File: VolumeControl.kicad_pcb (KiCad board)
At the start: 2 copper layers, 36 parts, among them J1 Input R/GND/L, J2 SPI, J4 5V Supply, J5 Lout, J6 Rout, J7 SubOut, U1 AD8400ARZ100, U2 AD8400ARZ100, U3 TL082, U4 TL082

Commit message: ähhhh
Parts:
- moved J4 128.4 mm to (27.4, 32.5), turned to 180 degrees
- moved C2 95.9 mm to (161.5, 30.5), turned to -90 degrees
- moved C3 89.6 mm to (135.4, 39.1), turned to 180 degrees
- moved C1 86.5 mm to (147.9, 24.4), turned to 90 degrees
- moved R2 84.6 mm to (128.5, 31.5)
- moved R1 82.1 mm to (138.7, 23.9), turned to 180 degrees
- moved R3 80.3 mm to (142.2, 33.5), turned to 90 degrees
- moved R4 78.2 mm to (151.9, 40.6)
- moved J1 70.5 mm to (161.4, 24.4), turned to 180 degrees
- moved R14 67.8 mm to (139.3, 104.9), turned to 180 degrees
- moved C4 66.6 mm to (42.4, 38.6), turned to 180 degrees
- moved C7 63.7 mm to (84.7, 33.5), turned to 90 degrees
- moved R12 59.2 mm to (80.9, 36.2), turned to 180 degrees
- moved U1 59.2 mm to (78.7, 59.9)
- moved C6 58.9 mm to (116.9, 124.0)
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
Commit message: uf
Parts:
- moved C2 29.5 mm to (135.2, 17.3), turned to 0 degrees
- moved R2 29.2 mm to (146.8, 54.2), turned to 90 degrees
- moved C7 26.3 mm to (72.6, 56.9)
- moved C8 26.3 mm to (72.6, 48.5)
- moved R12 26.3 mm to (68.8, 59.6)
- moved R13 26.3 mm to (58.3, 41.7)
- moved C3 20.8 mm to (154.4, 47.4), turned to -90 degrees
- moved R1 20.2 mm to (139.2, 44.0), turned to -90 degrees
- moved PS1 18.6 mm to (52.9, 36.5)
- moved C1 13.3 mm to (139.7, 34.8), turned to 180 degrees
- moved J1 12.5 mm to (148.9, 24.4), turned to -90 degrees
- moved R4 10.0 mm to (157.0, 32.0), turned to 90 degrees
- moved R3 9.59 mm to (148.8, 40.5), turned to 180 degrees
- moved U1 7.55 mm to (84.3, 54.9)
- moved U3 7.55 mm to (93.7, 84.1)
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
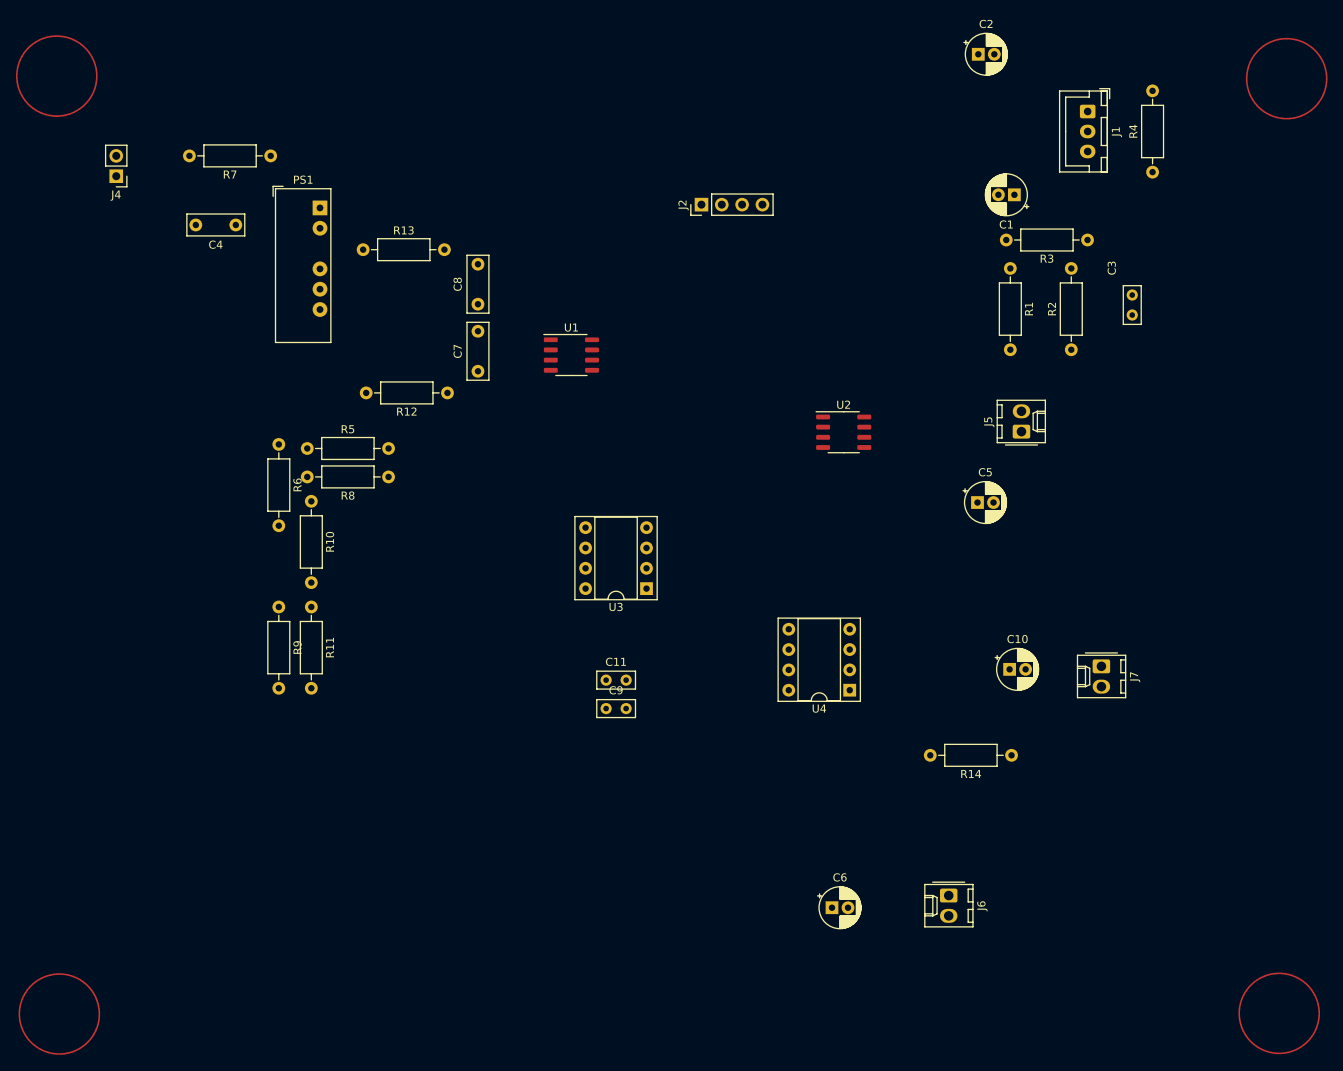
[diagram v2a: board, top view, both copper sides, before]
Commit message: corrected some issues in the schematic * added jumper for phase invert of the sub out * routed layout
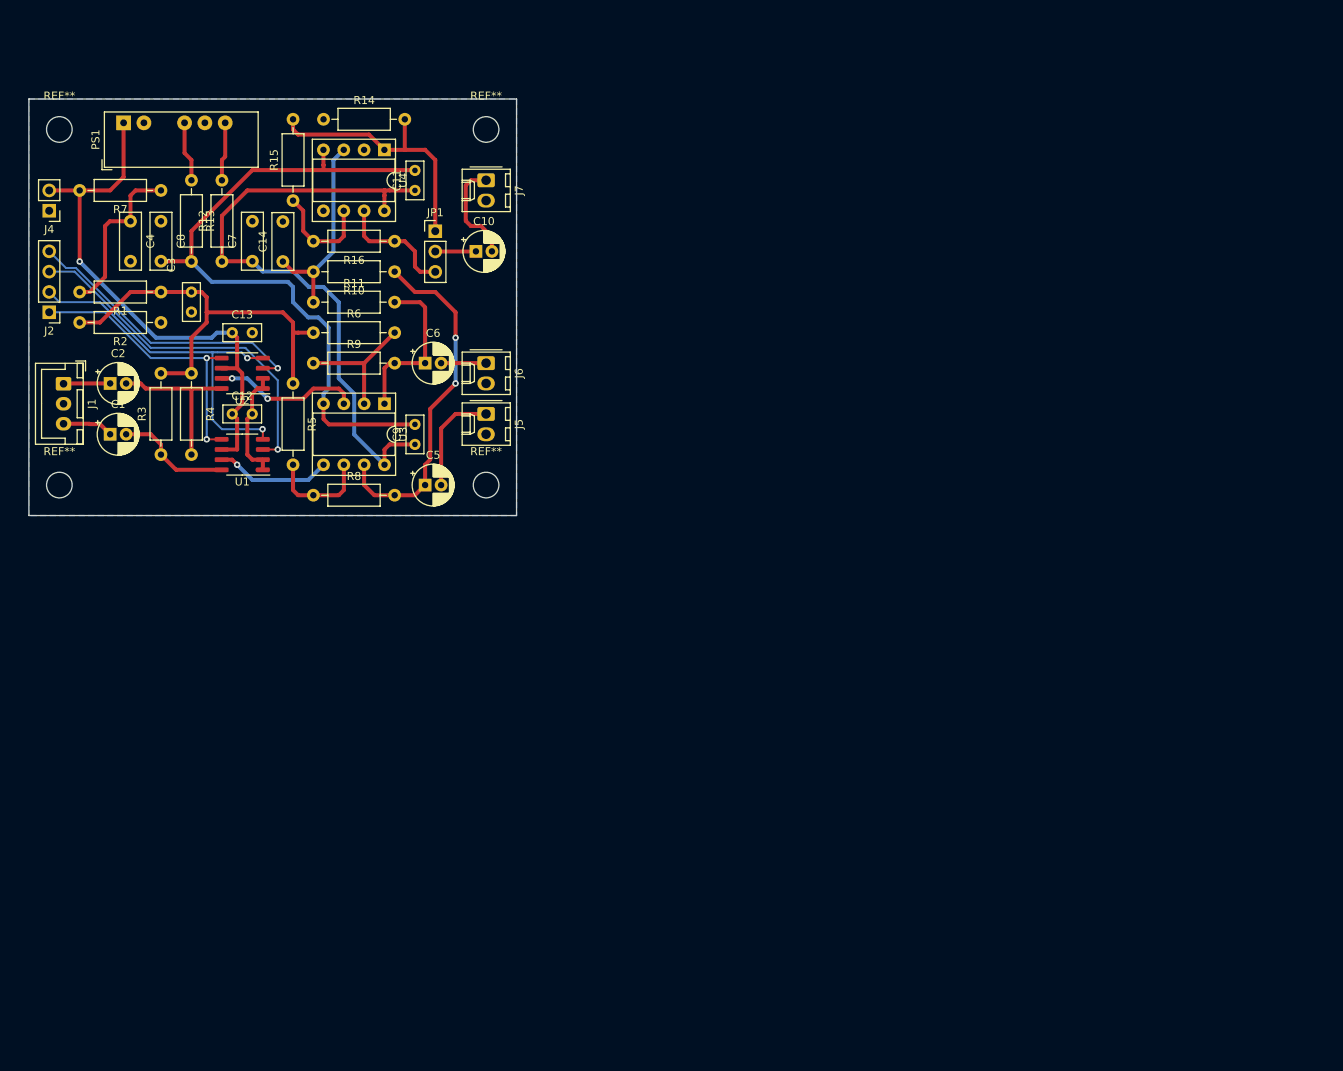
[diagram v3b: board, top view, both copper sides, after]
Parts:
- added C12: 100n, Capacitor_THT:C_Rect_L4.6mm_W2.0mm_P2.50mm_MKS02_FKP02, F.Cu at (41.9, 62.2)
- added C13: 100n, Capacitor_THT:C_Rect_L4.6mm_W2.0mm_P2.50mm_MKS02_FKP02, F.Cu at (41.9, 52.1)
- added C14: n.b., Capacitor_THT:C_Rect_L7.0mm_W2.5mm_P5.00mm, F.Cu at (48.3, 43.2)
- added JP1: Sub out invert select, Connector_PinHeader_2.54mm:PinHeader_1x03_P2.54mm_Vertical, F.Cu at (67.3, 39.4)
- added R15: 10K, Resistor_THT:R_Axial_DIN0207_L6.3mm_D2.5mm_P10.16mm_Horizontal, F.Cu at (49.5, 35.6)
- added R16: 10K, Resistor_THT:R_Axial_DIN0207_L6.3mm_D2.5mm_P10.16mm_Horizontal, F.Cu at (62.2, 40.6)
- added REF**: MountingHole_3.2mm_M3, MountingHole:MountingHole_3.2mm_M3, F.Cu at (73.7, 71.1)
- added REF**: MountingHole_3.2mm_M3, MountingHole:MountingHole_3.2mm_M3, F.Cu at (20.3, 71.1)
- added REF**: MountingHole_3.2mm_M3, MountingHole:MountingHole_3.2mm_M3, F.Cu at (73.7, 26.7)
- added REF**: MountingHole_3.2mm_M3, MountingHole:MountingHole_3.2mm_M3, F.Cu at (20.3, 26.7)
- moved J1 132.5 mm to (20.8, 58.5)
- moved R4 122.7 mm to (36.8, 57.1), turned to -90 degrees
- moved R3 118.9 mm to (33.0, 67.3), turned to 90 degrees
- moved C3 117.6 mm to (36.8, 47.0)
- moved R14 117.1 mm to (53.3, 25.4), turned to 0 degrees
- moved C1 116.9 mm to (26.7, 64.8), turned to 0 degrees
- moved C2 116.1 mm to (26.7, 58.4)
- moved R2 113.8 mm to (33.0, 50.8), turned to 180 degrees
- moved R1 106.2 mm to (33.0, 47.0), turned to 180 degrees
- moved J7 98.0 mm to (73.7, 33.0)
- moved U4 89.1 mm to (61.0, 29.2), turned to -90 degrees
- moved J6 88.2 mm to (73.7, 55.9)
- moved C6 85.0 mm to (66.0, 55.9)
- moved C10 84.7 mm to (72.4, 41.9)
- moved J2 82.6 mm to (19.1, 49.5), turned to 180 degrees
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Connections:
- C11 pad 1: Net-(C11-Pad1) -> +12VA
- C11 pad 2: Net-(C11-Pad2) -> -12VA
- C3 pad 1: Net-(C3-Pad1) -> mid
- C9 pad 1: Net-(C11-Pad1) -> +12VA
- C9 pad 2: Net-(C11-Pad2) -> -12VA
- J2 pad 2: /SDA -> /SDI
- R1 pad 1: Net-(C3-Pad1) -> mid
- R14 pad 2: Net-(C10-Pad1) -> Net-(R15-Pad2)
- R2 pad 2: Net-(C3-Pad1) -> mid
- R3 pad 2: Net-(C3-Pad1) -> mid
- R4 pad 1: Net-(C3-Pad1) -> mid
- R5 pad 1: GND -> mid
- R6 pad 1: GND -> mid
- U3 pad 4: Net-(C11-Pad2) -> -12VA
- U3 pad 8: Net-(C11-Pad1) -> +12VA
- U4 pad 1: Net-(C10-Pad1) -> Net-(R15-Pad2)
- U4 pad 4: Net-(C11-Pad2) -> -12VA
- U4 pad 5: -12VA -> GND
- U4 pad 6: +12VA -> Net-(U4-Pad6)
- U4 pad 7: unconnected-(U4-Pad7) -> Net-(U4-Pad7)
- U4 pad 8: Net-(C11-Pad1) -> +12VA
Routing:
- net -12VA: track 0.00 -> 86.4 mm
- net +12VA: track 0.00 -> 79.1 mm
- net +5V: track 0.00 -> 68.7 mm, vias 0 -> 1
- net mid: track 0.00 -> 53.3 mm
- net /SDI: track 0.00 -> 46.6 mm, vias 0 -> 2
- net /CS1: track 0.00 -> 44.7 mm, vias 0 -> 1
- net Net-(C5-Pad1): track 0.00 -> 44.1 mm, vias 0 -> 2
- net /CS2: track 0.00 -> 36.5 mm, vias 0 -> 1
- net /CLK: track 0.00 -> 36.0 mm, vias 0 -> 2
- net Net-(R15-Pad2): track 0.00 -> 33.4 mm
- net Net-(R10-Pad2): track 0.00 -> 25.0 mm
- net +5VA: track 0.00 -> 21.0 mm
- net Net-(C6-Pad1): track 0.00 -> 20.8 mm
- net Net-(C2-Pad2): track 0.00 -> 20.5 mm
- net Net-(U2-Pad7): track 0.00 -> 18.4 mm, vias 0 -> 2
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- added copper zone on B.Cu, net GND
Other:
- board outline added: 61 x 52.1 mm

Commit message: Added some Labels
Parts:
- moved J5 18.6 mm to (88.0, 50.4)
- moved J6 18.4 mm to (88.0, 44.3)
- moved R10 16.4 mm to (76.6, 36.4)
- moved R16 16.4 mm to (76.6, 32.6)
- moved C9 16.4 mm to (79.1, 58.0)
- moved C13 16.4 mm to (56.3, 44.0)
- moved C14 16.4 mm to (62.6, 35.1)
- moved C3 16.4 mm to (51.2, 38.9)
- moved J7 16.4 mm to (88.0, 25.0)
- moved R12 16.4 mm to (55.0, 35.1)
- moved R13 16.4 mm to (51.2, 25.0)
- moved REF** 16.4 mm to (88.0, 18.6)
- moved Ref** 16.4 mm to (88.0, 63.1)
- moved U1 16.4 mm to (57.5, 59.2)
- moved C10 16.4 mm to (86.7, 33.9)
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- renumbered REF** to Ref**
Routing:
- net /CS2: track 36.5 -> 41.4 mm
- net /CS1: track 44.7 -> 49.6 mm
- net /CLK: track 36.0 -> 40.9 mm
- net +5V: track 68.7 -> 73.7 mm
- net /SDI: track 46.6 -> 51.5 mm
- net Net-(C2-Pad1): track 5.84 -> 10.1 mm
- net Net-(C5-Pad2): track 13.4 -> 15.6 mm
- net Net-(C1-Pad1): track 6.37 -> 8.51 mm
- net Net-(C6-Pad2): track 5.62 -> 7.09 mm
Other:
- board size 61 x 52.1 mm -> 66.5 x 52.1 mm
- board text added: "5v/GND"
- board text added: "G/Lout"
- board text added: "G/Sout"
- board text added: "SPI"
- board text added: "VControl1 Idee von xasz Arbeit von Brainhunter"

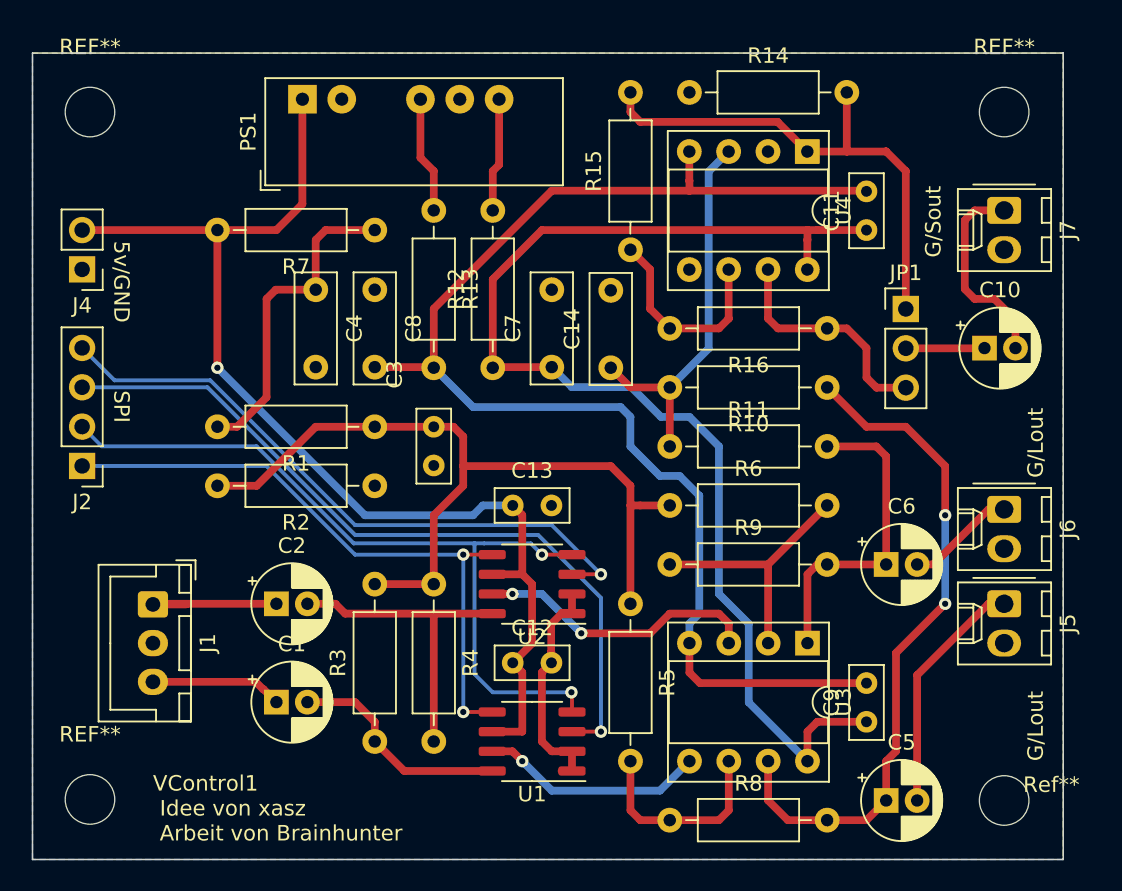
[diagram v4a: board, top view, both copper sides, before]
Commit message: changed design to AD5290
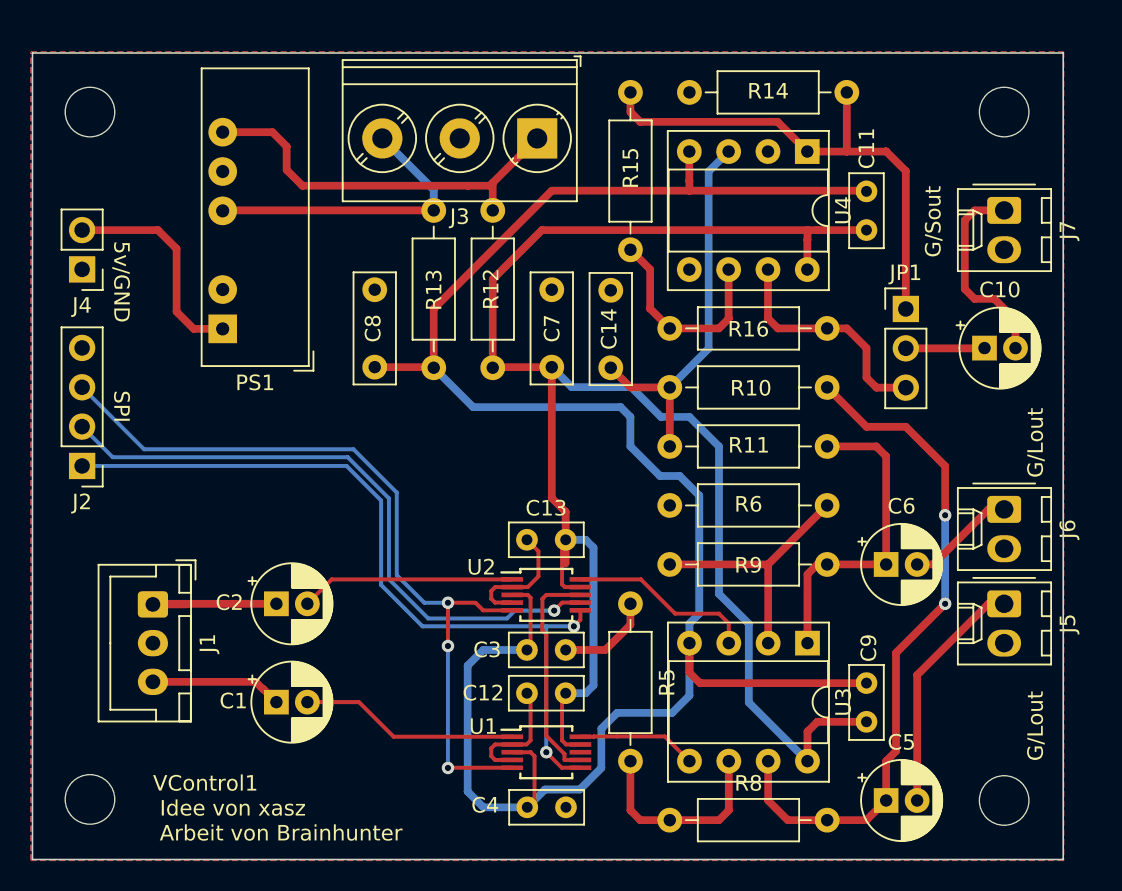
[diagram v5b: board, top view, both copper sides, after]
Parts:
- removed R1, R2, R3, R4: 100k, Resistor_THT:R_Axial_DIN0207_L6.3mm_D2.5mm_P10.16mm_Horizontal
- removed R7: 100, Resistor_THT:R_Axial_DIN0207_L6.3mm_D2.5mm_P10.16mm_Horizontal
- added J3: Screw_Terminal_01x03, TerminalBlock_Phoenix:TerminalBlock_Phoenix_PT-1,5-3-5.0-H_1x03_P5.00mm_Horizontal, F.Cu at (57.8, 20.3)
- C4: value 1u -> 100n; footprint Capacitor_THT:C_Rect_L7.0mm_W2.5mm_P5.00mm -> Capacitor_THT:C_Rect_L4.6mm_W2.0mm_P2.50mm_MKS02_FKP02
- U1, U2: value AD8400ARZ100 -> AD5290; footprint Package_SO:SO-8_3.9x4.9mm_P1.27mm -> Package_SO:MSOP-10_3x3mm_P0.5mm
- moved C4 37.1 mm to (59.7, 63.5), turned to 180 degrees
- moved C3 16.7 mm to (59.7, 53.3), turned to 180 degrees
- moved PS1 15.7 mm to (37.5, 32.6), turned to 180 degrees
- moved C13 4.07 mm to (59.7, 46.2), turned to 180 degrees
- moved C12 3.94 mm to (59.7, 56.1), turned to 180 degrees
- moved U1 1.15 mm to (58.4, 59.9), turned to 0 degrees
- moved U2 1.15 mm to (58.4, 49.8), turned to 0 degrees
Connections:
- C12 pad 1: +5V -> +12VA
- C13 pad 1: +5V -> +12VA
- C3 pad 1: mid -> GND
- C3 pad 2: GND -> -12VA
- C4 pad 1: +5VA -> GND
- C4 pad 2: GND -> -12VA
- J2 pad 4: /CS2 -> GND
- R5 pad 1: mid -> GND
- R6 pad 1: mid -> GND
- U1 pad 1: GND -> Net-(C1-Pad2)
- U1 pad 3: /CS1 -> -12VA
- U1 pad 4: /SDI -> GND
- U1 pad 5: /CLK -> /CS1
- U1 pad 6: +5V -> /CLK
- U1 pad 7: Net-(U1-Pad7) -> Net-(U2-Pad8)
- U1 pad 8: Net-(C1-Pad2) -> unconnected-(U1-Pad8)
- U2 pad 1: GND -> Net-(C2-Pad2)
- U2 pad 3: /CS2 -> -12VA
- U2 pad 4: /SDI -> GND
- U2 pad 5: /CLK -> /CS1
- U2 pad 6: +5V -> /CLK
- U2 pad 7: Net-(U2-Pad7) -> /SDI
- U2 pad 8: Net-(C2-Pad2) -> Net-(U2-Pad8)
- U3 pad 3: Net-(U2-Pad7) -> Net-(U3-Pad3)
- U3 pad 5: Net-(U1-Pad7) -> Net-(U1-Pad10)
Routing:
- net +5V: track 73.7 -> 14.1 mm, vias 1 -> 0
- net mid: track 53.3 -> 0.00 mm
- net -12VA: track 86.4 -> 131.1 mm
- net /CS2: track 41.4 -> 0.00 mm, vias 1 -> 0
- net +12VA: track 79.1 -> 113.7 mm
- net +5VA: track 21.0 -> 0.00 mm
- net Net-(U2-Pad7): track 18.4 -> 0.00 mm, vias 2 -> 0
- net Net-(J3-Pad1): track 7.35 -> 25.7 mm
- net Net-(U1-Pad7): track 14.6 -> 0.00 mm, vias 1 -> 0
- net Net-(U2-Pad8): track 0.00 -> 14.6 mm
- net Net-(PS1-Pad4): track 7.54 -> 19.7 mm
- net Net-(U3-Pad3): track 0.00 -> 12.0 mm
- net /SDI: track 51.5 -> 40.8 mm, vias 2 -> 1
- net /CLK: track 40.9 -> 51.2 mm
- net Net-(U1-Pad10): track 0.00 -> 7.71 mm
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- added copper zone on F.Cu, net GND
